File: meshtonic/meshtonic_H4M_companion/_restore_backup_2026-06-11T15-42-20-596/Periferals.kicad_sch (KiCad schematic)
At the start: 15 parts, among them J18 Micro_SD_Card_passive_clk, U10 CR2013-MI2120, U11 MCP23017x-x-SS

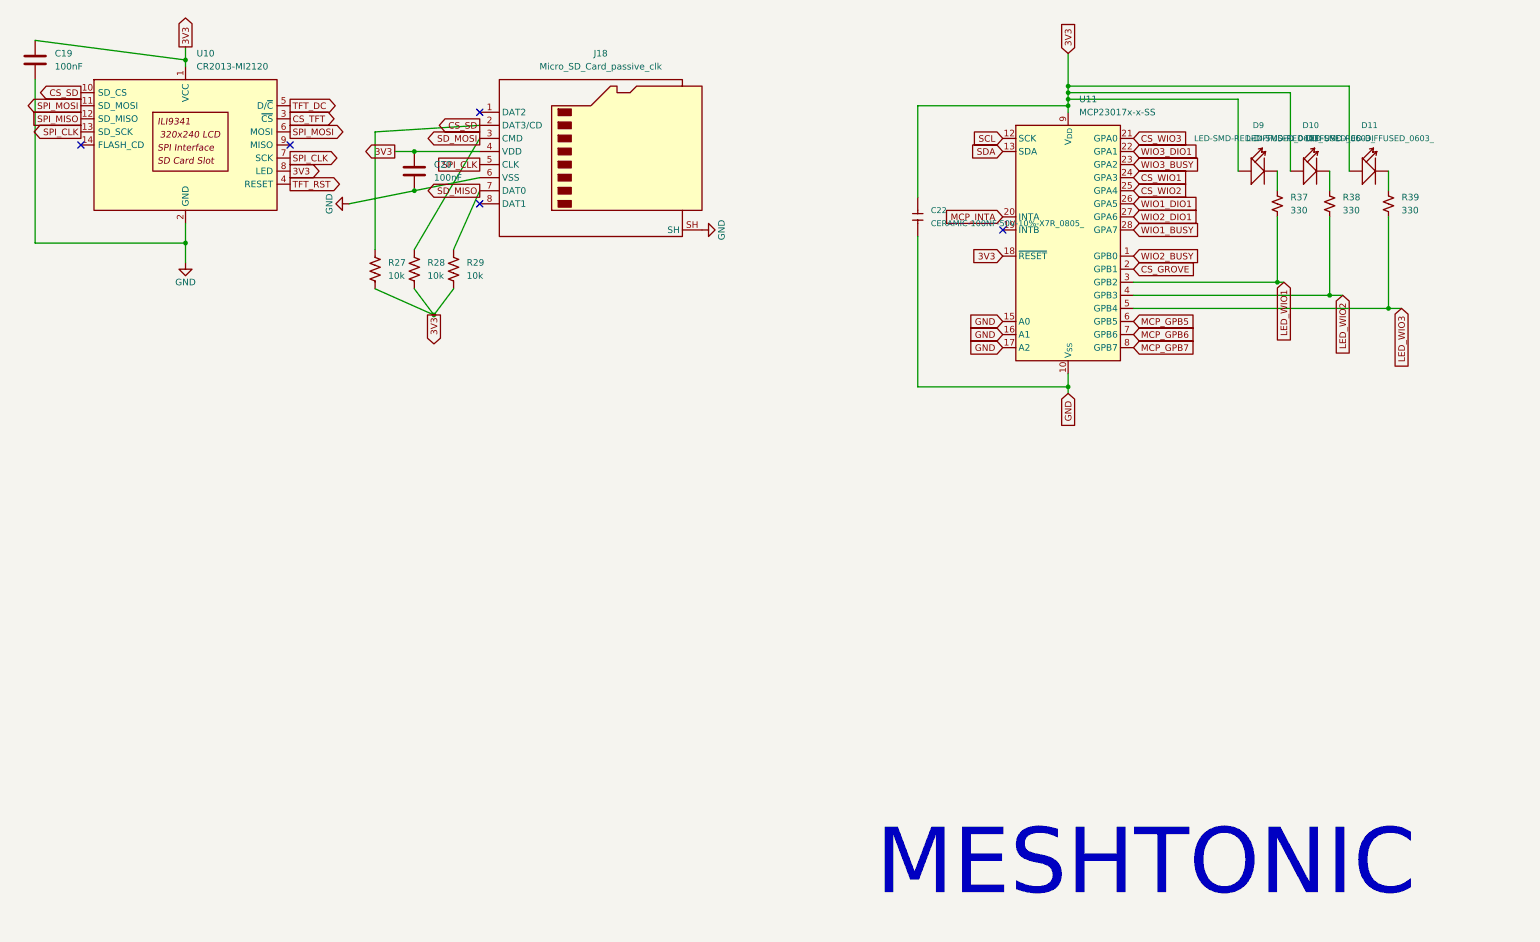
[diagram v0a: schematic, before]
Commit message: adds meshtonic board
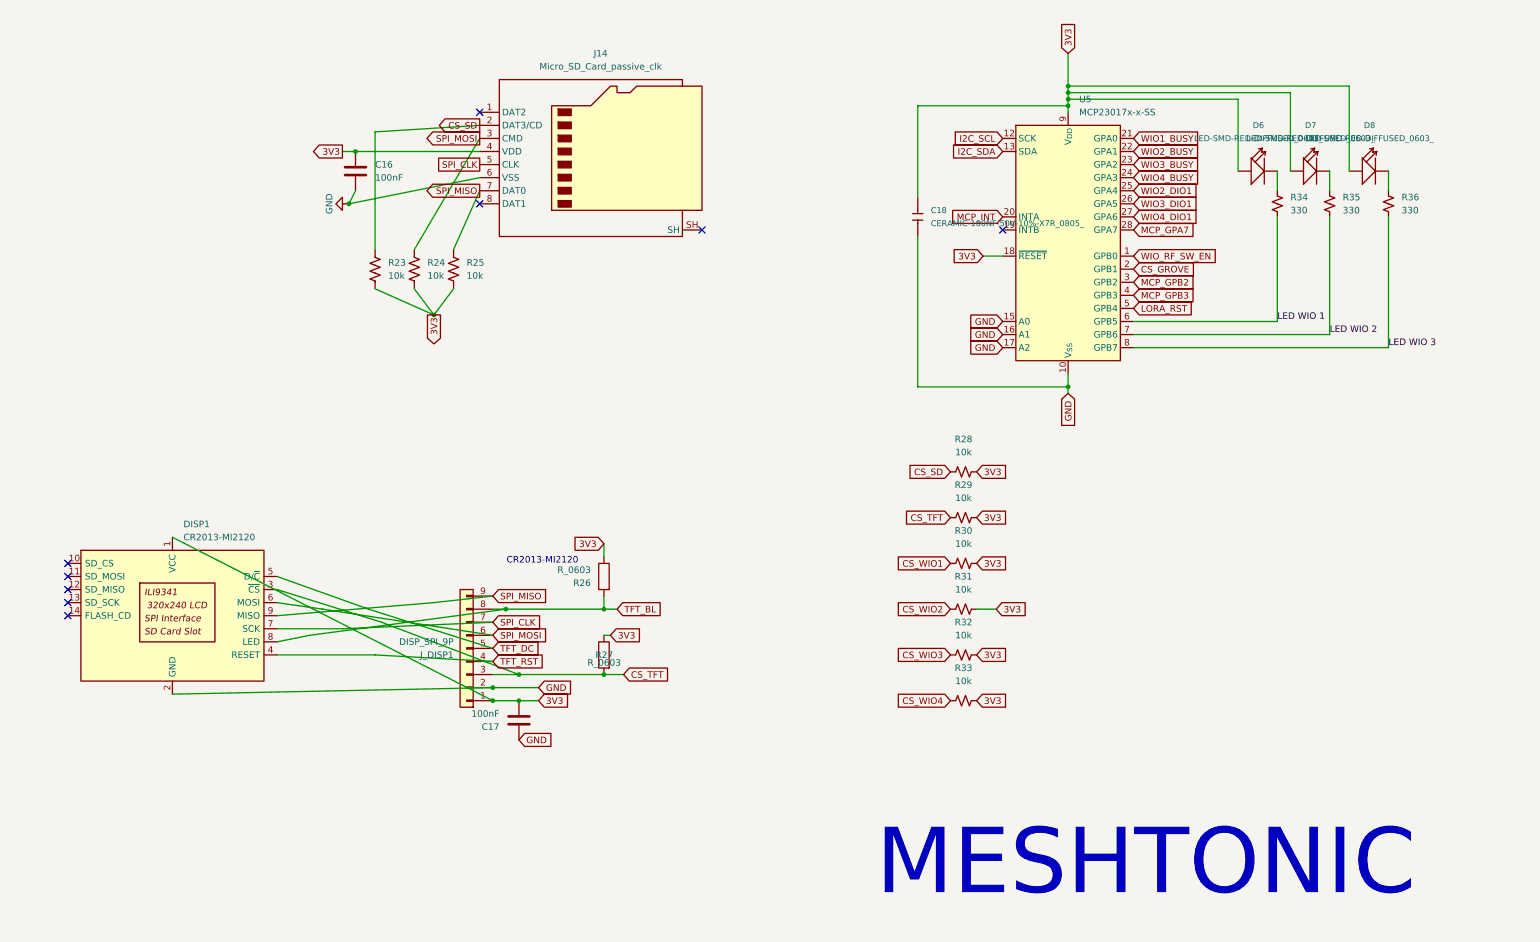
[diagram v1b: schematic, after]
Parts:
- added DISP1: CR2013-MI2120, symbol Driver_Display:CR2013-MI2120
- added R26, R27: R_0603, PCM_Resistor_SMD_AKL:R_0603_1608Metric, symbol PCM_Resistor_AKL:R_0603
- added R28, R29, R30, R31, R32, R33: 10k, PCM_SparkFun-Resistor:R_0603_1608Metric, symbol PCM_SparkFun-Resistor:10k_0603
- C18: renamed from C22; footprint (none) -> Capacitor_SMD:C_0805_2012Metric
- J_DISP1: renamed from U10; value CR2013-MI2120 -> DISP_SPI_9P; footprint Display:CR2013-MI2120 -> Connector_PinHeader_2.54mm:PinHeader_1x09_P2.54mm_Vertical; symbol Driver_Display:CR2013-MI2120 -> Connector_Generic:Conn_01x09
- renumbered C20 to C16, C19 to C17, D9 to D6, D10 to D7, D11 to D8, J18 to J14, R27 to R23, R28 to R24, R29 to R25, R37 to R34, R38 to R35, R39 to R36, U11 to U5
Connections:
- net MCP_GPB5 is gone; now on net LED WIO 1: U5.6 (GPB5)
- net MCP_GPB6 is gone; now on net LED WIO 2: U5.7 (GPB6)
- net MCP_GPB7 is gone; now on net LED WIO 3: U5.8 (GPB7)
- net SD_MISO is gone; now on net SPI_MISO: J14.7 (DAT0), R25.1
- net SD_MOSI is gone; now on net SPI_MOSI: J14.3 (CMD), R24.1
- net WIO1_DIO1 is gone; now on net WIO3_DIO1: U5.26 (GPA5)
- net 3V3: now also C17.2, DISP1.1 (VCC), R26.2, R27.2, R28.2, R29.2, R30.2, R31.2, R32.2, R33.2; no longer C17.1, J_DISP1.8 (LED)
- net CS_SD: now also R28.1; no longer J_DISP1.10 (SD_CS)
- net CS_TFT: now also DISP1.3 (~{CS}), R27.1, R29.1
- net CS_WIO1: now also R30.1; no longer U5.24 (GPA3)
- net CS_WIO2: now also R31.1; no longer U5.25 (GPA4)
- net CS_WIO3: now also R32.1; no longer U5.21 (GPA0)
- net GND: now also C17.1, DISP1.2 (GND); no longer C17.2, J14.SH
- net SPI_CLK: now also DISP1.7 (SCK); no longer J_DISP1.13 (SD_SCK)
- net SPI_MISO: now also J_DISP1.9 (MISO), DISP1.9 (MISO); no longer J_DISP1.12 (SD_MISO)
- net SPI_MOSI: now also DISP1.6 (MOSI); no longer J_DISP1.11 (SD_MOSI)
- net TFT_DC: now also DISP1.5 (D/~{C})
- net TFT_RST: now also DISP1.4 (RESET)
- net WIO1_BUSY: now also U5.21 (GPA0); no longer U5.28 (GPA7)
- net WIO2_BUSY: now also U5.22 (GPA1); no longer U5.1 (GPB0)
- net WIO2_DIO1: now also U5.25 (GPA4); no longer U5.27 (GPA6)
- net WIO3_DIO1: no longer U5.22 (GPA1)
- net LED_WIO1 renamed LED WIO 1
- net LED WIO 1: no longer U5.3 (GPB2)
- net LED_WIO2 renamed LED WIO 2
- net LED WIO 2: no longer U5.4 (GPB3)
- net LED_WIO3 renamed LED WIO 3
- net LED WIO 3: no longer U5.5 (GPB4)
- net MCP_INTA renamed MCP_INT
- net SCL renamed I2C_SCL
- net SDA renamed I2C_SDA
- new net CS_WIO4: R33.1
- new net LORA_RST: U5.5 (GPB4)
- new net MCP_GPA7: U5.28 (GPA7)
- new net MCP_GPB2: U5.3 (GPB2)
- new net MCP_GPB3: U5.4 (GPB3)
- new net TFT_BL: DISP1.8 (LED), J_DISP1.8 (LED), R26.1
- new net WIO4_BUSY: U5.24 (GPA3)
- new net WIO4_DIO1: U5.27 (GPA6)
- new net WIO_RF_SW_EN: U5.1 (GPB0)
- no-connect marks 5 -> 9
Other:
- note added: "CR2013-MI2120"
- moved on the sheet: C16, C17
